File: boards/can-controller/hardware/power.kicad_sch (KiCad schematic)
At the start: 16 parts, among them J20 12V IN, Q1 SUD50P04-08, U20 R-78E5.0-0.5, U21 TLP293

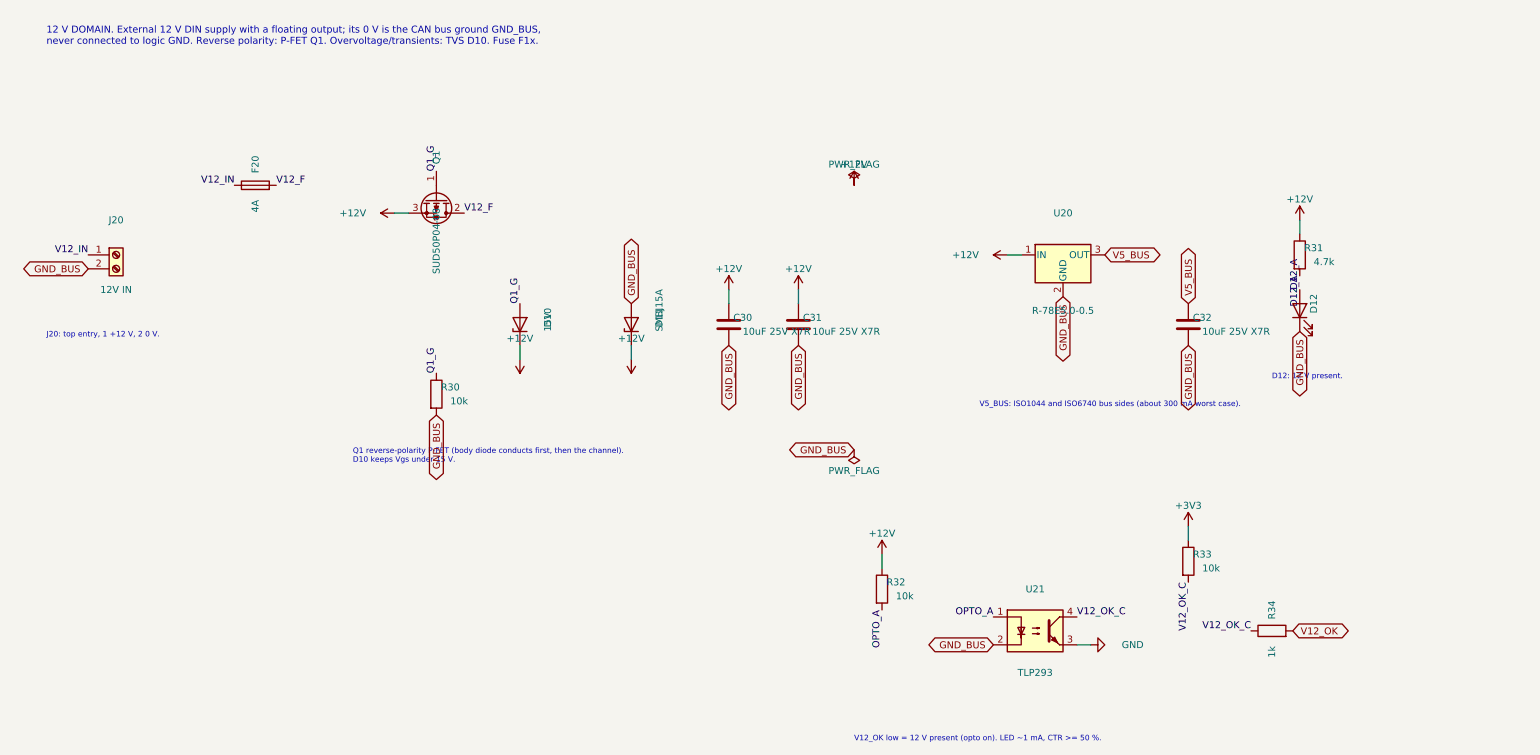
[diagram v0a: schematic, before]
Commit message: can-controller: schematic for the new scope (Ethernet W6100, 4 x ISOW1044, AQW212 relays, diff AI)
Six sheets generated by gen_schematic.py: MCU and logic power, Ethernet,
CAN x4, 12 V input and isolated logic supply (TDN 5-2411WI), relay drive,
GPIO and analog in. ERC 0; netlist check: no net crosses a domain except
at the designed crossings. New lib parts: Thl_Interface:W6100-L (flat),
Thl_Isolator:AQW212, stock ISOW1044 / TDN 5WI / LQFP-48 / bead footprints.
PCB still holds the old layout (next: update from schematic, placement).

Co-Authored-By: Claude Opus 5.5 <noreply@anthropic.com>
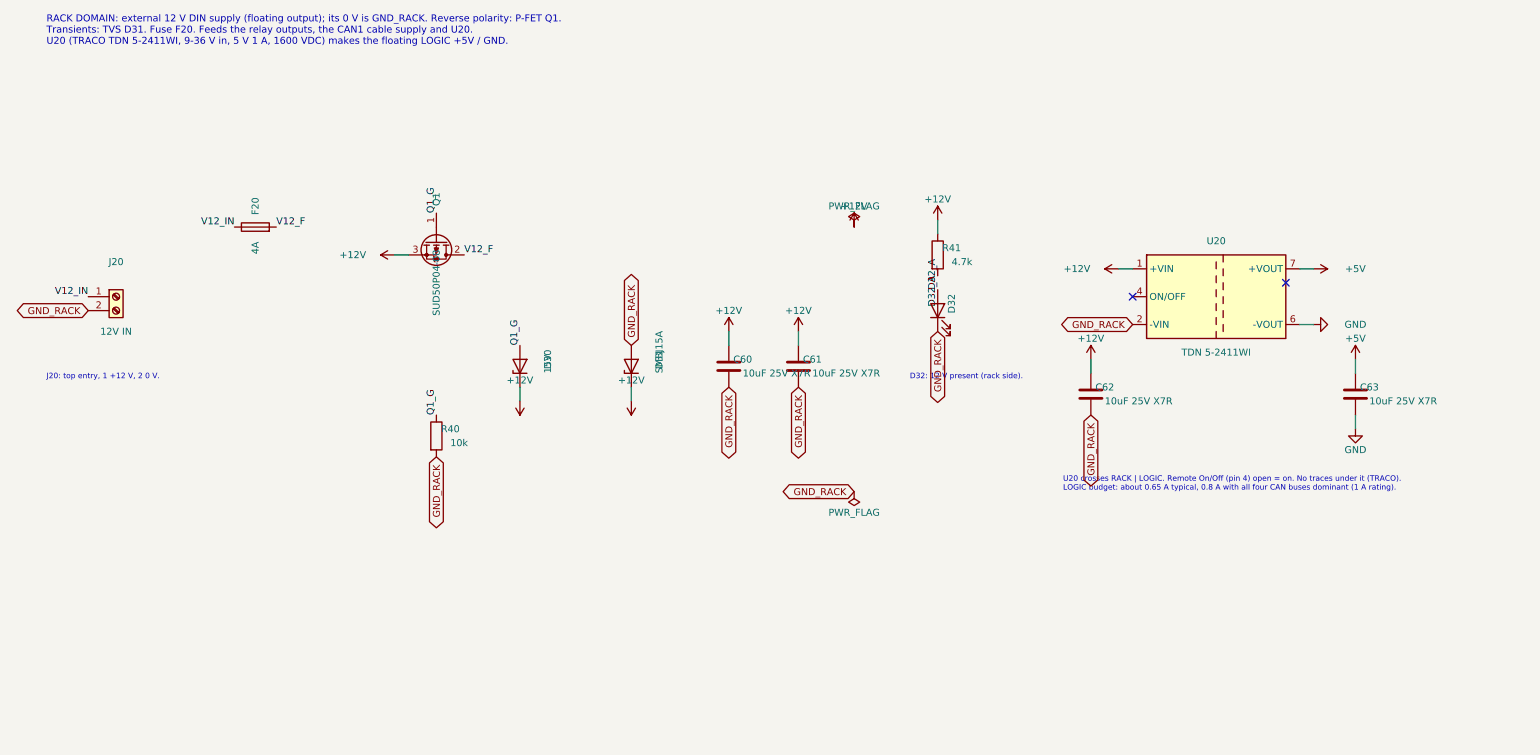
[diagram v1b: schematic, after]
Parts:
- removed C30, C31, C32: 10uF 25V X7R, Capacitor_SMD:C_1206_3216Metric_Pad1.33x1.80mm_HandSolder, symbol Device:C
- removed D10: 15V, Diode_SMD:D_SOD-123, symbol Device:D_Zener
- removed D11: SMBJ15A, Diode_SMD:D_SMB_Handsoldering, symbol Device:D_Zener
- removed D12: LED green, LED_SMD:LED_1206_3216Metric_Pad1.42x1.75mm_HandSolder, symbol Device:LED
- removed R30, R32, R33: 10k, Resistor_SMD:R_1206_3216Metric_Pad1.30x1.75mm_HandSolder, symbol Device:R
- removed R31: 4.7k, Resistor_SMD:R_1206_3216Metric_Pad1.30x1.75mm_HandSolder, symbol Device:R
- removed R34: 1k, Resistor_SMD:R_1206_3216Metric_Pad1.30x1.75mm_HandSolder, symbol Device:R
- removed U20: R-78E5.0-0.5, Converter_DCDC:Converter_DCDC_RECOM_R-78E-0.5_THT, symbol Converter_DCDC:R-78E5.0-0.5
- removed U21: TLP293, Package_SO:SOIC-4_4.55x2.6mm_P1.27mm, symbol Isolator:TLP291
- added C60, C61, C62, C63: 10uF 25V X7R, Capacitor_SMD:C_1206_3216Metric_Pad1.33x1.80mm_HandSolder, symbol Device:C
- added D30: 15V, Diode_SMD:D_SOD-123, symbol Device:D_Zener
- added D31: SMBJ15A, Diode_SMD:D_SMB_Handsoldering, symbol Device:D_Zener
- added D32: LED green, LED_SMD:LED_1206_3216Metric_Pad1.42x1.75mm_HandSolder, symbol Device:LED
- added R40: 10k, Resistor_SMD:R_1206_3216Metric_Pad1.30x1.75mm_HandSolder, symbol Device:R
- added R41: 4.7k, Resistor_SMD:R_1206_3216Metric_Pad1.30x1.75mm_HandSolder, symbol Device:R
- added U20: TDN 5-2411WI, Converter_DCDC:Converter_DCDC_TRACO_TDN_5-xxxxWI_THT, symbol Regulator_Switching:TDN_5-0910WISM
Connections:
- net +12V: now also C60.1, C61.1, C62.1, D30.1 (K), D31.1 (K), R41.1, U20.1 (+VIN)
- net GND: now also C63.2, U20.6 (-VOUT)
- net Q1_G: now also D30.2 (A), R40.1
- net GND_BUS renamed GND_RACK
- net GND_RACK: now also C60.2, C61.2, C62.2, D31.2 (A), D32.1 (K), R40.2, U20.2 (-VIN)
- new net +5V: C63.1, U20.7 (+VOUT)
- new net D32_A: D32.2 (A), R41.2
- no-connect marks 0 -> 2
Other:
- note added: "D32: 12 V present (rack side)."
- note added: "RACK DOMAIN: external 12 V DIN supply (floating output); its 0 V is GND_RACK. Reverse polarity: P-FET Q1. Transients: TVS D31. Fuse F20. Feeds the relay outputs, the CAN1 cable supply and U20. U20 (TRACO TDN 5-2411WI, 9-36 V in, 5 V 1 A, 1600 VDC) makes the floating LOGIC +5V / GND."
- note added: "U20 crosses RACK | LOGIC. Remote On/Off (pin 4) open = on. No traces under it (TRACO). LOGIC budget: about 0.65 A typical, 0.8 A with all four CAN buses dominant (1 A rating)."
- note removed: "12 V DOMAIN. External 12 V DIN supply with a floating output; its 0 V is the CAN bus ground GND_BUS, never connected to logic GND. Reverse polarity: P-FET Q1. Overvoltage/transients: TVS D10. Fuse F1x."
- note removed: "D12: 12 V present."
- note removed: "Q1 reverse-polarity P-FET (body diode conducts first, then the channel). D10 keeps Vgs under 15 V."
- note removed: "V12_OK low = 12 V present (opto on). LED ~1 mA, CTR >= 50 %."
- note removed: "V5_BUS: ISO1044 and ISO6740 bus sides (about 300 mA worst case)."
- title: CAN controller: 12 V input, bus-side 5 V, 12 V status -> CAN controller: 12 V input and isolated logic supply

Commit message: Move core, can-card, io-card, serial-card, can-ssr, probe-helper to rev B
Rev A went to PCBWay and is tagged revA. Rev B replaces parts the Mouser
BOM check flagged (obsolete, end of life, not recommended for new designs,
or not orderable) and swaps out-of-stock passives and diodes for in-stock
equivalents. Field-only changes, same footprints, no layout change; the
reference boards (can-controller, pic-module) get the same part numbers.
The rev A order lists (DigiKey, Mouser) carry the same substitutions; the
Mouser list leaves out the T821 box headers (bought from DigiKey).

docs/rev-b-changes.md lists every change and the rev B to-dos (MAX7219 is
obsolete and must be replaced). transfer/mouser-revA.xlsx (Mouser BOM
check) consumed.

Co-Authored-By: Claude Opus 5.5 <noreply@anthropic.com>
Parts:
- C60, C61, C62, C63: MPN GRM31CR71E106KA12L -> CL31B106KAHNNNE; Manufacturer Murata -> Samsung Electro-Mechanics
- D32: MPN LTST-C150GKT -> LTST-C150KGKT
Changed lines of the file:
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@@
 			)
 		)
-		(property "Manufacturer" "Murata"
+		(property "Manufacturer" "Samsung Electro-Mechanics"
 			(at 149.86 83.82 0)
 			(hide yes)
@@
 			)
 		)
-		(property "MPN" "GRM31CR71E106KA12L"
+		(property "MPN" "CL31B106KAHNNNE"
 			(at 149.86 83.82 0)
 			(hide yes)
@@
 			)
 		)
-		(property "Manufacturer" "Murata"
+		(property "Manufacturer" "Samsung Electro-Mechanics"
 			(at 162.56 83.82 0)
 			(hide yes)
@@
 			)
 		)
-		(property "MPN" "GRM31CR71E106KA12L"
+		(property "MPN" "CL31B106KAHNNNE"
 			(at 162.56 83.82 0)
 			(hide yes)
@@
 			)
 		)
-		(property "MPN" "LTST-C150GKT"
+		(property "MPN" "LTST-C150KGKT"
 			(at 187.96 73.66 0)
 			(hide yes)
@@
 			)
 		)
-		(property "Manufacturer" "Murata"
+		(property "Manufacturer" "Samsung Electro-Mechanics"
 			(at 215.9 88.9 0)
 			(hide yes)
@@
 			)
 		)
-		(property "MPN" "GRM31CR71E106KA12L"
+		(property "MPN" "CL31B106KAHNNNE"
 			(at 215.9 88.9 0)
 			(hide yes)
@@
 			)
 		)
-		(property "Manufacturer" "Murata"
+		(property "Manufacturer" "Samsung Electro-Mechanics"
 			(at 264.16 88.9 0)
 			(hide yes)
@@
 			)
 		)
-		(property "MPN" "GRM31CR71E106KA12L"
+		(property "MPN" "CL31B106KAHNNNE"
 			(at 264.16 88.9 0)
 			(hide yes)

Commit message: Rev B / rev A order: 10 uF CL31B106KAHZW6E, beads BLM31PG391SN1L
Both earlier substitutes (CL31B106KAHNNNE, BLM31KN102SH1L) are on
backorder at Mouser. CL31B106KAHZW6E has the same rating (1.4 mm tall).
The isolated-supply beads need no 1 kOhm: TI's reference uses 330 Ohm;
BLM31PG391SN1L is 390 Ohm @ 100 MHz, 2 A, 50 mOhm. Field-only changes;
order lists regenerated.

Co-Authored-By: Claude Opus 5.5 <noreply@anthropic.com>
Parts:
- C60, C61, C62, C63: MPN CL31B106KAHNNNE -> CL31B106KAHZW6E
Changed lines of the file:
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@@
 			)
 		)
-		(property "MPN" "CL31B106KAHNNNE"
+		(property "MPN" "CL31B106KAHZW6E"
 			(at 149.86 83.82 0)
 			(hide yes)
@@
 			)
 		)
-		(property "MPN" "CL31B106KAHNNNE"
+		(property "MPN" "CL31B106KAHZW6E"
 			(at 162.56 83.82 0)
 			(hide yes)
@@
 			)
 		)
-		(property "MPN" "CL31B106KAHNNNE"
+		(property "MPN" "CL31B106KAHZW6E"
 			(at 215.9 88.9 0)
 			(hide yes)
@@
 			)
 		)
-		(property "MPN" "CL31B106KAHNNNE"
+		(property "MPN" "CL31B106KAHZW6E"
 			(at 264.16 88.9 0)
 			(hide yes)

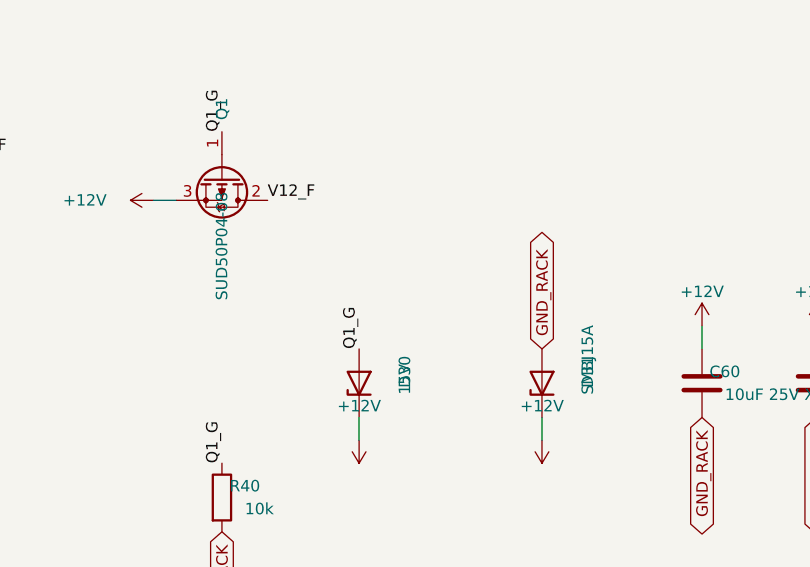
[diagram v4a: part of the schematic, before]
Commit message: Mouser cart: SQD50P04-09L P-FET, Diotec P6SMBJ15A TVS
Out of stock: Vishay SUD50P04-08-GE3 (core Q1) -> SQD50P04-09L_GE3 and
Littelfuse SMBJ15A (12 V input TVS) -> Diotec P6SMBJ15A, same footprints,
in core, can-ssr and the can-controller/pic-module references. Logged in
docs/rev-b-changes.md; order lists regenerated. The cart as ordered is
docs/orders/mouser-cart-2026-10-12.xls.

Co-Authored-By: Claude Opus 5.5 <noreply@anthropic.com>
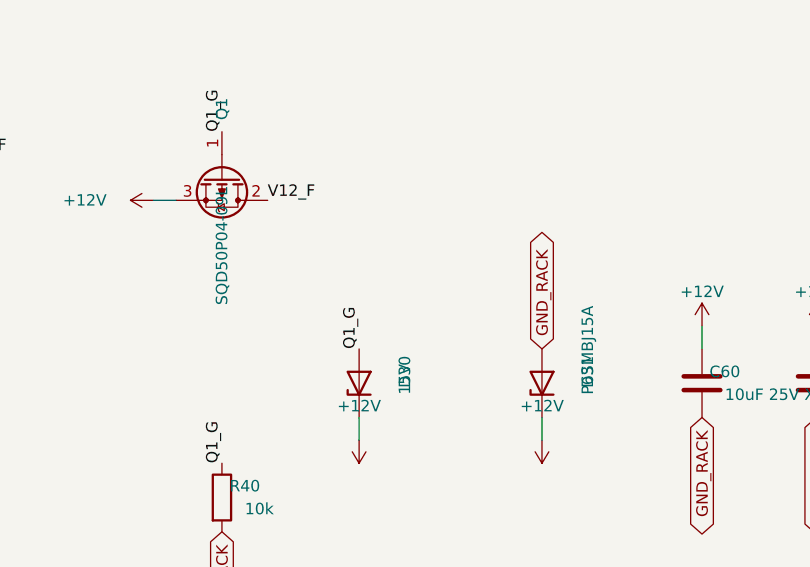
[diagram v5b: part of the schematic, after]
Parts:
- D31: value SMBJ15A -> P6SMBJ15A; MPN SMBJ15A -> P6SMBJ15A; Manufacturer Littelfuse -> Diotec Semiconductor
- Q1: value SUD50P04-08 -> SQD50P04-09L; MPN SUD50P04-08-GE3 -> SQD50P04-09L_GE3
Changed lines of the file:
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@@
 			)
 		)
-		(property "Value" "SUD50P04-08"
+		(property "Value" "SQD50P04-09L"
 			(at 96.52 68.58 0)
 			(effects
@@
 			)
 		)
-		(property "MPN" "SUD50P04-08-GE3"
+		(property "MPN" "SQD50P04-09L_GE3"
 			(at 96.52 60.96 0)
 			(hide yes)
@@
 			)
 		)
-		(property "Value" "SMBJ15A"
+		(property "Value" "P6SMBJ15A"
 			(at 137.16 85.09 0)
 			(effects
@@
 			)
 		)
-		(property "Manufacturer" "Littelfuse"
+		(property "Manufacturer" "Diotec Semiconductor"
 			(at 132.08 83.82 0)
 			(hide yes)
@@
 			)
 		)
-		(property "MPN" "SMBJ15A"
+		(property "MPN" "P6SMBJ15A"
 			(at 132.08 83.82 0)
 			(hide yes)
